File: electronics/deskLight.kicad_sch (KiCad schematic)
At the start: 57 parts, among them J1 Conn_01x03_Pin, J2 Conn_01x16_Pin, J3 Conn_01x05, Q1 2n7002, Q10 IRF540NS, Q11 IRF540NS, Q12 IRF540NS, Q13 IRF540NS, Q14 IRF540NS, Q15 IRF540NS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

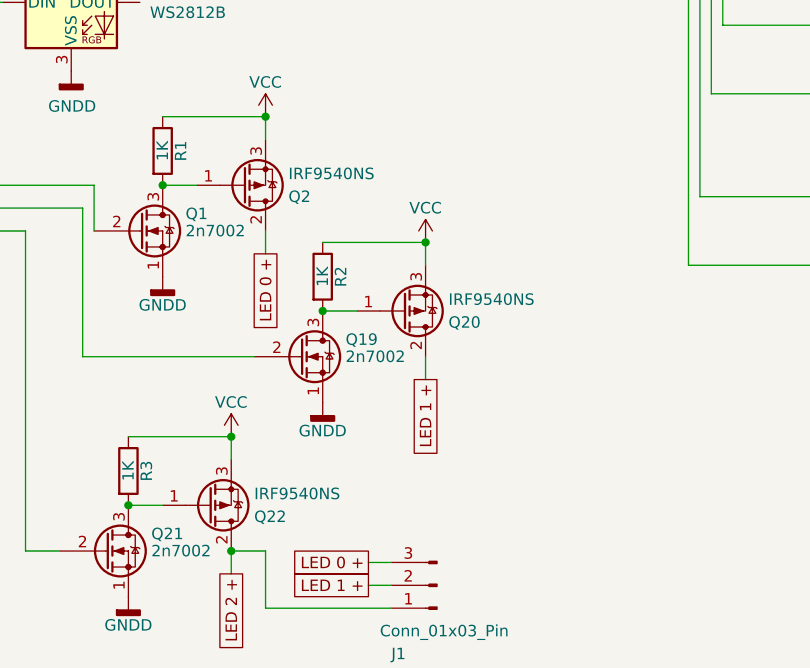
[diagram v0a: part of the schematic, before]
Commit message: Added LCSC part P-channel MOSFET
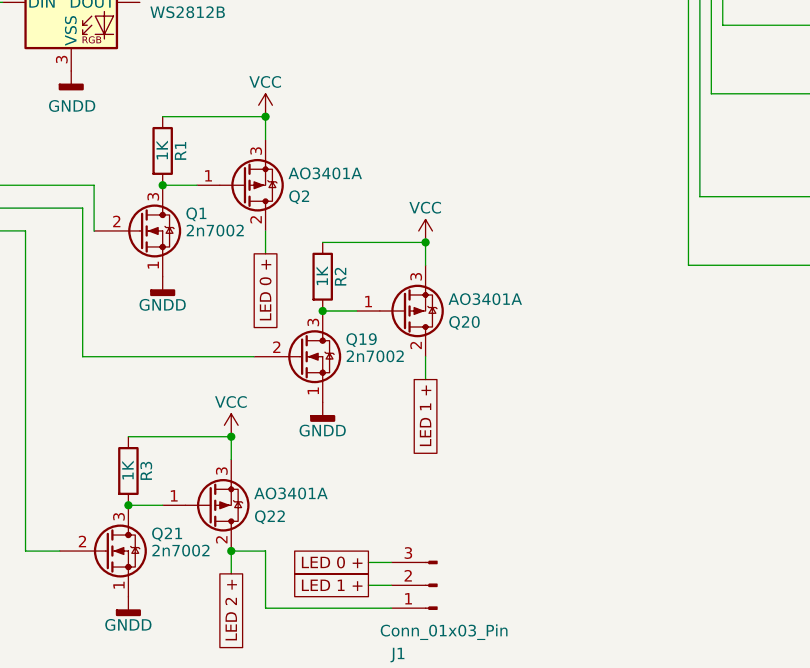
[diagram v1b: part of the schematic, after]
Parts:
- Q2, Q20, Q22: value IRF9540NS -> AO3401A; footprint TO_SOT_Packages_SMD:TO-263-2 -> Package_TO_SOT_SMD:SOT-23; LCSC (none) -> C15127; Note (none) -> https://jlcpcb.com/partdetail/Alpha_OmegaSemicon-AO3401A/C1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
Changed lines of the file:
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@@
     (comment 4 "PCB version using the wroom board")
   )
-  (junction (at 140.97 184.15) (diameter 0) (color 0 0 0 0)
-  )
   (junction (at 133.35 143.51) (diameter 0) (color 0 0 0 0)
   )
@@
   (junction (at 100.33 173.99) (diameter 0) (color 0 0 0 0)
   )
+  (junction (at 140.97 184.15) (diameter 0) (color 0 0 0 0)
+  )
   (junction (at 125.73 48.26) (diameter 0) (color 0 0 0 0)
   )
@@
       (effects (font (size 1.27 1.27)) (justify left))
     )
-    (property "Value" "IRF9540NS" (at 147.32 142.24 0)
+    (property "Value" "AO3401A " (at 147.32 142.24 0)
       (effects (font (size 1.27 1.27)) (justify left))
     )
-    (property "Footprint" "TO_SOT_Packages_SMD:TO-263-2" (at 147.32 146.05 0)
+    (property "Footprint" "Package_TO_SOT_SMD:SOT-23" (at 147.32 146.05 0)
       (effects (font (size 1.27 1.27)) hide)
     )
@@
       (effects (font (size 1.27 1.27)) hide)
     )
+    (property "Note" "https://jlcpcb.com/partdetail/Alpha_OmegaSemicon-AO3401A/C15127 " (at 142.24 143.51 0)
+      (effects (font (size 1.27 1.27)) hide)
+    )
+    (property "LCSC" "C15127" (at 142.24 143.51 0)
+      (effects (font (size 1.27 1.27)) hide)
+    )
     (pin "1")
     (pin "2")
@@
     )
   )
-  (symbol (lib_id "Device:Q_PMOS_GDS") (at 160.02 157.48 0) (mirror x) (unit 1)
-    (in_bom yes) (on_board yes) (dnp no)
-    (property "Reference" "Q20" (at 165.1 158.75 0)
-      (effects (font (size 1.27 1.27)) (justify left))
-    )
-    (property "Value" "IRF9540NS" (at 165.1 156.21 0)
-      (effects (font (size 1.27 1.27)) (justify left))
-    )
-    (property "Footprint" "TO_SOT_Packages_SMD:TO-263-2" (at 165.1 160.02 0)
-      (effects (font (size 1.27 1.27)) hide)
-    )
-    (property "Datasheet" "" (at 160.02 157.48 0)
-      (effects (font (size 1.27 1.27)) hide)
-    )
-    (pin "1")
-    (pin "2")
-    (pin "3")
-    (instances
-      (project "deskLight"
-        (path "/b32f9917-42b1-4401-9b92-791f624b2b40"
-          (reference "Q20") (unit 1)
-        )
-      )
-    )
-  )
   (symbol (lib_id "Device:R") (at 74.93 158.75 0) (unit 1)
     (in_bom yes) (on_board yes) (dnp no)
@@
     )
   )
+  (symbol (lib_id "Device:Q_PMOS_GDS") (at 160.02 157.48 0) (mirror x) (unit 1)
+    (in_bom yes) (on_board yes) (dnp no)
+    (property "Reference" "Q20" (at 165.1 158.75 0)
+      (effects (font (size 1.27 1.27)) (justify left))
+    )
+    (property "Value" "AO3401A " (at 165.1 156.21 0)
+      (effects (font (size 1.27 1.27)) (justify left))
+    )
+    (property "Footprint" "Package_TO_SOT_SMD:SOT-23" (at 165.1 160.02 0)
+      (effects (font (size 1.27 1.27)) hide)
+    )
+    (property "Datasheet" "" (at 160.02 157.48 0)
+      (effects (font (size 1.27 1.27)) hide)
+    )
+    (property "Note" "https://jlcpcb.com/partdetail/Alpha_OmegaSemicon-AO3401A/C15127 " (at 160.02 157.48 0)
+      (effects (font (size 1.27 1.27)) hide)
+    )
+    (property "LCSC" "C15127" (at 160.02 157.48 0)
+      (effects (font (size 1.27 1.27)) hide)
+    )
+    (pin "1")
+    (pin "2")
+    (pin "3")
+    (instances
+      (project "deskLight"
+        (path "/b32f9917-42b1-4401-9b92-791f624b2b40"
+          (reference "Q20") (unit 1)
+        )
+      )
+    )
+  )
   (symbol (lib_id "transistors:2N7000") (at 127 184.15 0) (unit 1)
     (in_bom yes) (on_board yes) (dnp no)
@@
       (effects (font (size 1.27 1.27)) (justify left))
     )
-    (property "Value" "IRF9540NS" (at 143.51 177.8 0)
+    (property "Value" "AO3401A " (at 143.51 177.8 0)
       (effects (font (size 1.27 1.27)) (justify left))
     )
-    (property "Footprint" "TO_SOT_Packages_SMD:TO-263-2" (at 143.51 181.61 0)
+    (property "Footprint" "Package_TO_SOT_SMD:SOT-23" (at 143.51 181.61 0)
       (effects (font (size 1.27 1.27)) hide)
     )
@@
       (effects (font (size 1.27 1.27)) hide)
     )
+    (property "Note" "https://jlcpcb.com/partdetail/Alpha_OmegaSemicon-AO3401A/C15127 " (at 138.43 179.07 0)
+      (effects (font (size 1.27 1.27)) hide)
+    )
+    (property "LCSC" "C15127" (at 138.43 179.07 0)
+      (effects (font (size 1.27 1.27)) hide)
+    )

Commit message: Made some decisions
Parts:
- added R1 (x19): 10k, Resistor_SMD:R_0805_2012Metric_Pad1.20x1.40mm_HandSolder, symbol Device:R
- C1: footprint (none) -> Capacitor_SMD:C_0805_2012Metric_Pad1.18x1.45mm_HandSolder; LCSC (none) -> C720961
- Q1, Q19, Q21: value 2n7002 -> 2N7002PW; LCSC (none) -> C7379955
- Q10, Q11, Q12, Q13, Q14, Q15, Q16, Q17, Q18, Q3, Q4, Q5, Q6, Q7, Q8, Q9: value IRF540NS -> 2302V; footprint TO_SOT_Packages_SMD:TO-263-2 -> Package_TO_SOT_SMD:SOT-23; LCSC (none) -> C7431443
- Q2, Q20, Q22: value AO3401A -> 4435B; footprint Package_TO_SOT_SMD:SOT-23 -> Package_SO:SOP-8_3.9x4.9mm_P1.27mm; LCSC C15127 -> C7431441; Note https://jlcpcb.com/partdetail/Alpha_OmegaSemicon-AO3401A/C1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 -> https://www.lcsc.com/product-detail/MOSFETs_HL-4435B_C74314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
- R1, R11, R12: LCSC (none) -> C3016734
- SW1: footprint (none) -> Rotary_Encoder:RotaryEncoder_Alps_EC11E-Switch_Vertical_H20mm
- U1: LCSC (none) -> C473012
- U2: LCSC (none) -> C92206
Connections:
- net LED 10 -: now also Q13.2 (D); no longer Q16.2 (D)
- net LED 11 -: now also Q14.2 (D); no longer Q9.2 (D)
- net LED 12 -: now also Q15.2 (D); no longer Q17.2 (D)
- net LED 13 -: now also Q16.2 (D); no longer Q10.2 (D)
- net LED 14 -: now also Q17.2 (D); no longer Q18.2 (D)
- net LED 15 -: now also Q18.2 (D); no longer Q11.2 (D)
- net LED 2 -: now also Q5.2 (D); no longer Q12.2 (D)
- net LED 3 -: now also Q6.2 (D); no longer Q5.2 (D)
- net LED 4 -: now also Q7.2 (D); no longer Q13.2 (D)
- net LED 5 -: now also Q8.2 (D); no longer Q6.2 (D)
- net LED 6 -: now also Q9.2 (D); no longer Q14.2 (D)
- net LED 7 -: now also Q10.2 (D); no longer Q7.2 (D)
- net LED 8 -: now also Q11.2 (D); no longer Q15.2 (D)
- net LED 9 -: now also Q12.2 (D); no longer Q8.2 (D)
- net at Q1.2 (G): now also R1.2; no longer U1.23 (IO15)
- net at Q3.1 (G): now also R1.2; no longer U2.6 (LED0)
- net at U2.10 (LED4): now also R1.1; no longer Q13.1 (G)
- net at U2.11 (LED5): now also R1.1; no longer Q6.1 (G)
- net at U2.12 (LED6): now also R1.1; no longer Q14.1 (G)
- net at U2.13 (LED7): now also R1.1; no longer Q7.1 (G)
- net at U2.15 (LED8): now also R1.1; no longer Q15.1 (G)
- net at U2.16 (LED9): now also R1.1; no longer Q8.1 (G)
- net at U2.17 (LED10): now also R1.1; no longer Q16.1 (G)
- net at U2.18 (LED11): now also R1.1; no longer Q9.1 (G)
- net at U2.19 (LED12): now also R1.1; no longer Q17.1 (G)
- net at U2.20 (LED13): now also R1.1; no longer Q10.1 (G)
- net at U2.21 (LED14): now also R1.1; no longer Q18.1 (G)
- net at U2.22 (LED15): now also R1.1; no longer Q11.1 (G)
- net at U2.7 (LED1): now also R1.1; no longer Q4.1 (G)
- net at U2.8 (LED2): now also R1.1; no longer Q12.1 (G)
- net at U2.9 (LED3): now also R1.1; no longer Q5.1 (G)
- net at U1.27 (IO16): now also R1.1; no longer Q19.2 (G)
- net at U1.28 (IO17): now also R1.1; no longer Q21.2 (G)
- new net: R1.1, U2.6 (LED0)
- new net: R1.1, U1.23 (IO15)
- new net: Q16.1 (G), R1.2
- new net: Q15.1 (G), R1.2
- new net: Q18.1 (G), R1.2
- new net: Q4.1 (G), R1.2
- new net: Q5.1 (G), R1.2
- new net: Q8.1 (G), R1.2
- new net: Q9.1 (G), R1.2
- new net: Q13.1 (G), R1.2
- new net: Q21.2 (G), R1.2
- new net: Q19.2 (G), R1.2
- new net: Q12.1 (G), R1.2
- new net: Q17.1 (G), R1.2
- new net: Q10.1 (G), R1.2
- new net: Q14.1 (G), R1.2
- new net: Q7.1 (G), R1.2
- new net: Q6.1 (G), R1.2
- new net: Q11.1 (G), R1.2

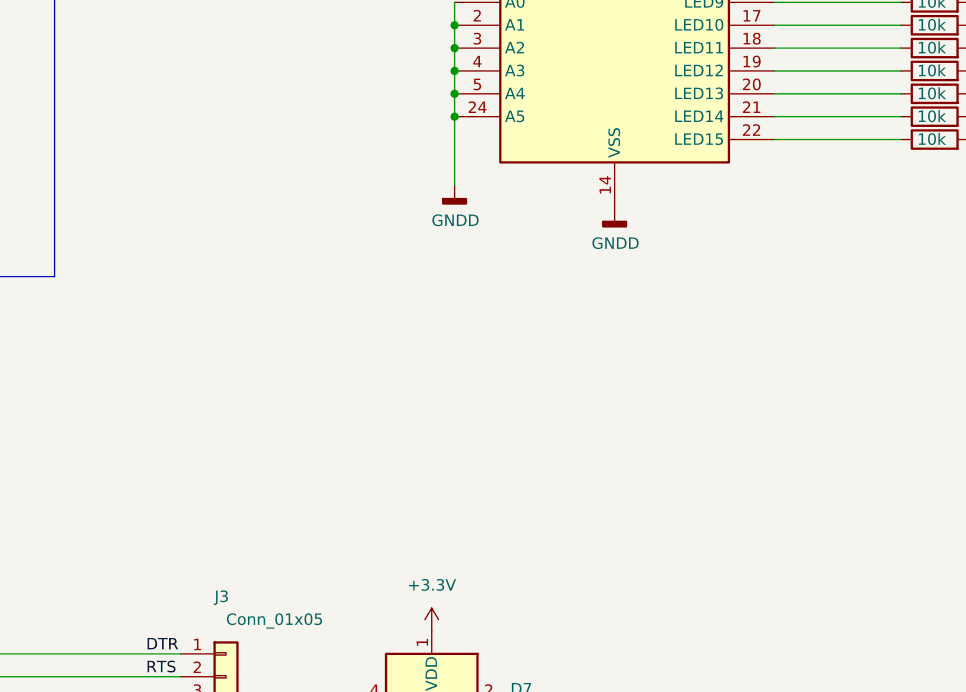
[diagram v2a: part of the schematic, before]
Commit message: Added step down converter
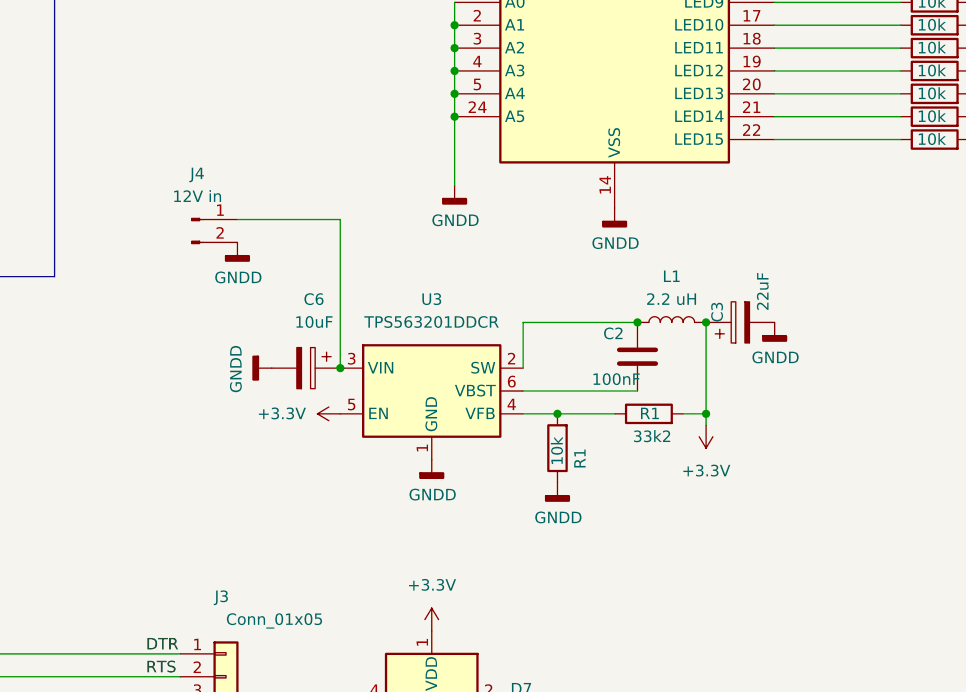
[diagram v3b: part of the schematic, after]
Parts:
- added C2: 100nF, Capacitor_SMD:C_0805_2012Metric_Pad1.18x1.45mm_HandSolder, symbol Device:C
- added C3: 22uF, symbol Device:C_Polarized
- added C6: 10uF, symbol Device:C_Polarized
- added J4: 12V in, symbol Connector:Conn_01x02_Pin
- added L1: 2.2 uH, symbol Device:L
- added R1: 10k, Resistor_SMD:R_0805_2012Metric_Pad1.20x1.40mm_HandSolder, symbol Device:R
- added R1: 33k2, Resistor_SMD:R_0805_2012Metric_Pad1.20x1.40mm_HandSolder, symbol Device:R
- added U3: TPS563201DDCR, Package_TO_SOT_SMD:SOT-23-6, symbol Regulator_Switching:TPS563200
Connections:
- net +3.3V: now also C3.1, L1.2, R1.2, U3.5 (EN)
- net GNDD: now also C3.2, C6.2, J4.2 (Pin_2), R1.1, U3.1 (GND)
- new net: R1.1, R1.2, U3.4 (VFB)
- new net: C2.1, L1.1, U3.2 (SW)
- new net: C6.1, J4.1 (Pin_1), U3.3 (VIN)
- new net: C2.2, U3.6 (VBST)

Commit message: Added step down converter
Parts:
- J3: value Conn_01x05 -> Programming
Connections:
- net Rx: now reaches J3.4 (Pin_4), U1.34 (RXD0/IO3)
- net Tx: now reaches J3.3 (Pin_3), U1.35 (TXD0/IO1)
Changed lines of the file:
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@@
+    (effects (font (size 1.27 1.27)) (justify left bottom))
+  )
+  (label "Rx" (at 91.44 125.73 0) (fields_autoplaced)
+    (effects (font (size 1.27 1.27)) (justify left bottom))
+  )
+  (label "Tx" (at 91.44 123.19 0) (fields_autoplaced)
     (effects (font (size 1.27 1.27)) (justify left bottom))
   )
@@
       (effects (font (size 1.27 1.27)) (justify left))
     )
-    (property "Value" "Conn_01x05" (at 100.33 114.3 0)
-      (effects (font (size 1.27 1.27)) (justify left))
-    )
+    (property "Value" "Programming" (at 99.06 114.3 0)
+      (effects (font (size 1.27 1.27)) (justify left))
+    )

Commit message: Gave NPN a value
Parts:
- Q23, Q24: value NPN -> BC817w; LCSC (none) -> C148104
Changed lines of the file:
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@@
   (symbol (lib_id "Simulation_SPICE:NPN") (at 31.75 106.68 90) (mirror x) (unit 1)
     (in_bom yes) (on_board yes) (dnp no)
-    (property "Reference" "Q23" (at 30.48 111.76 0)
-      (effects (font (size 1.27 1.27)) (justify left))
-    )
-    (property "Value" "NPN" (at 33.02 111.76 0)
+    (property "Reference" "Q23" (at 34.29 111.76 90)
+      (effects (font (size 1.27 1.27)) (justify left))
+    )
+    (property "Value" "BC817w" (at 38.1 114.3 90)
       (effects (font (size 1.27 1.27)) (justify left))
     )
@@
     )
     (property "Sim.Pins" "1=C 2=B 3=E" (at 31.75 106.68 0)
+      (effects (font (size 1.27 1.27)) hide)
+    )
+    (property "LCSC" "C148104" (at 31.75 106.68 0)
       (effects (font (size 1.27 1.27)) hide)
     )
@@
   (symbol (lib_id "Simulation_SPICE:NPN") (at 52.07 106.68 270) (unit 1)
     (in_bom yes) (on_board yes) (dnp no)
-    (property "Reference" "Q24" (at 53.34 111.76 0)
-      (effects (font (size 1.27 1.27)) (justify left))
-    )
-    (property "Value" "NPN" (at 50.8 111.76 0)
+    (property "Reference" "Q24" (at 49.53 111.76 90)
+      (effects (font (size 1.27 1.27)) (justify left))
+    )
+    (property "Value" "BC817w" (at 49.53 114.3 90)
       (effects (font (size 1.27 1.27)) (justify left))
     )
@@
       (effects (font (size 1.27 1.27)) hide)
     )
+    (property "LCSC" "C148104" (at 52.07 106.68 0)
+      (effects (font (size 1.27 1.27)) hide)
+    )

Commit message: Added NPN footprint
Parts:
- Q23, Q24: footprint (none) -> Package_TO_SOT_SMD:SOT-323_SC-70
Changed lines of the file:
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@@
       (effects (font (size 1.27 1.27)) (justify left))
     )
-    (property "Footprint" "" (at 31.75 170.18 0)
+    (property "Footprint" "Package_TO_SOT_SMD:SOT-323_SC-70" (at 31.75 170.18 0)
       (effects (font (size 1.27 1.27)) hide)
     )
@@
       (effects (font (size 1.27 1.27)) (justify left))
     )
-    (property "Footprint" "" (at 52.07 170.18 0)
-      (effects (font (size 1.27 1.27)) hide)
-    )
+    (property "Footprint" "Package_TO_SOT_SMD:SOT-323_SC-70" (at 52.07 170.18 0)
+      (effects (font (size 1.27 1.27)) hide)
+    )

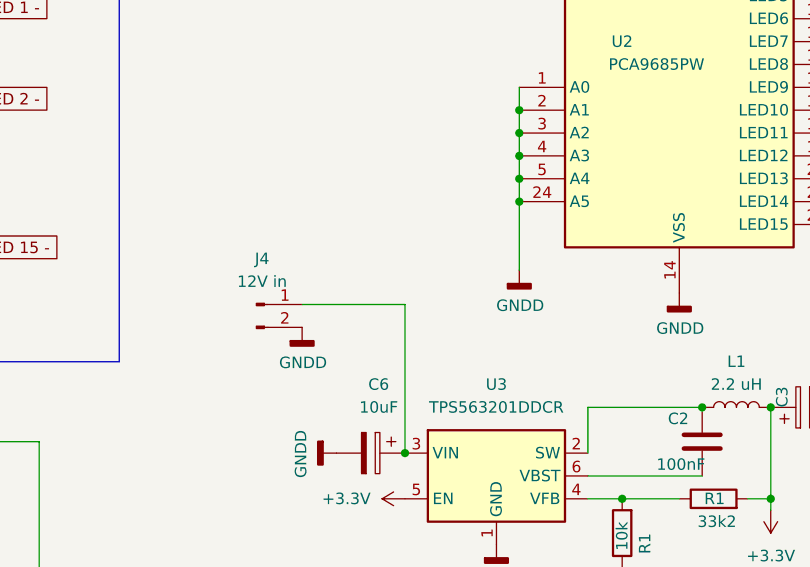
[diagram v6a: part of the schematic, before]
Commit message: Connected 12V in to VCC
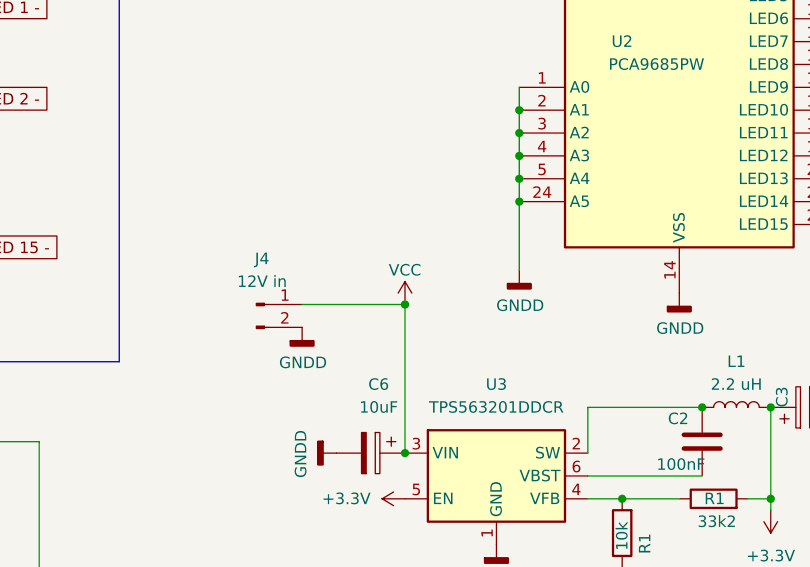
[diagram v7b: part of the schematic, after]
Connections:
- net VCC: now also C6.1, J4.1 (Pin_1), U3.3 (VIN)
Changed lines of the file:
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@@
   (junction (at 74.93 163.83) (diameter 0) (color 0 0 0 0)
+  )
+  (junction (at 113.03 69.85) (diameter 0) (color 0 0 0 0)
   )
   (junction (at 125.73 50.8) (diameter 0) (color 0 0 0 0)
@@
         )
       )
+    )
+  )
+  (symbol (lib_id "power:VCC") (at 113.03 69.85 0) (unit 1)
+    (in_bom yes) (on_board yes) (dnp no)
+    (property "Reference" "#PWR030" (at 113.03 73.66 0)
+      (effects (font (size 1.27 1.27)) hide)
+    )
+    (property "Value" "VCC" (at 113.03 66.04 0)
+      (effects (font (size 1.27 1.27)))
+    )
+    (property "Footprint" "" (at 113.03 69.85 0)
+      (effects (font (size 1.27 1.27)) hide)
+    )
+    (property "Datasheet" "" (at 113.03 69.85 0)
+      (effects (font (size 1.27 1.27)) hide)
+    )
+    (pin "1")
+    (instances
+      (project "deskLight"
+        (path "/b32f9917-42b1-4401-9b92-791f624b2b40"
+          (reference "#PWR030") (unit 1)
+        )
+      )

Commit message: Added 2.2uH from LCSC
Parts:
- L1: footprint (none) -> Inductor_SMD_Wurth:L_Wurth_WE-LQSH-2010; LCMC (none) -> C315717
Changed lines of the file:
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@@
       (effects (font (size 1.27 1.27)))
     )
-    (property "Footprint" "" (at 149.86 81.28 0)
+    (property "Footprint" "Inductor_SMD_Wurth:L_Wurth_WE-LQSH-2010" (at 149.86 81.28 0)
       (effects (font (size 1.27 1.27)) hide)
     )
-    (property "Datasheet" "~" (at 149.86 81.28 0)
+    (property "Datasheet" "https://datasheet.lcsc.com/lcsc/2304140030_INPAQ-WIP201610P-2R2ML_C315717.pdf" (at 149.86 81.28 0)
       (effects (font (size 1.27 1.27)) hide)
     )
+    (property "LCMC" "C315717" (at 149.86 81.28 90)
+      (effects (font (size 1.27 1.27)) hide)
+    )
